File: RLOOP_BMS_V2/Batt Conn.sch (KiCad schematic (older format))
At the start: 1 part, among them J2 2-640387-0

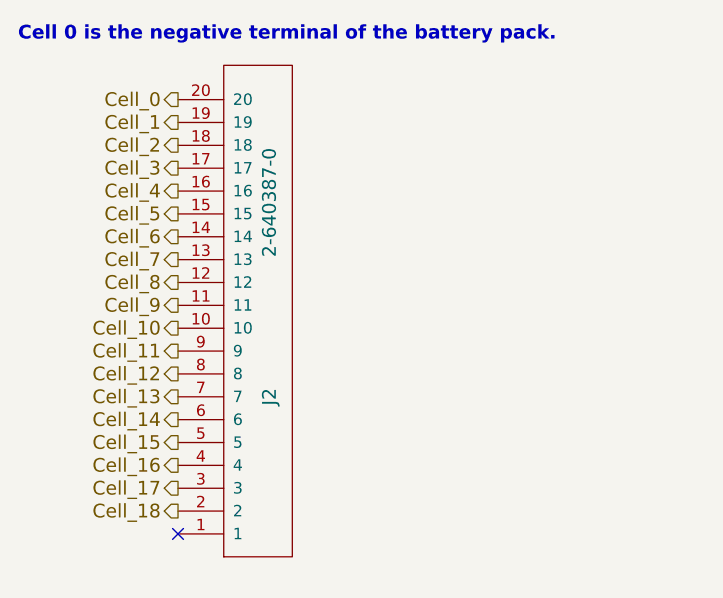
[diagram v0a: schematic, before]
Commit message: swapped a few connectors to standardize with the power node and what's readily available
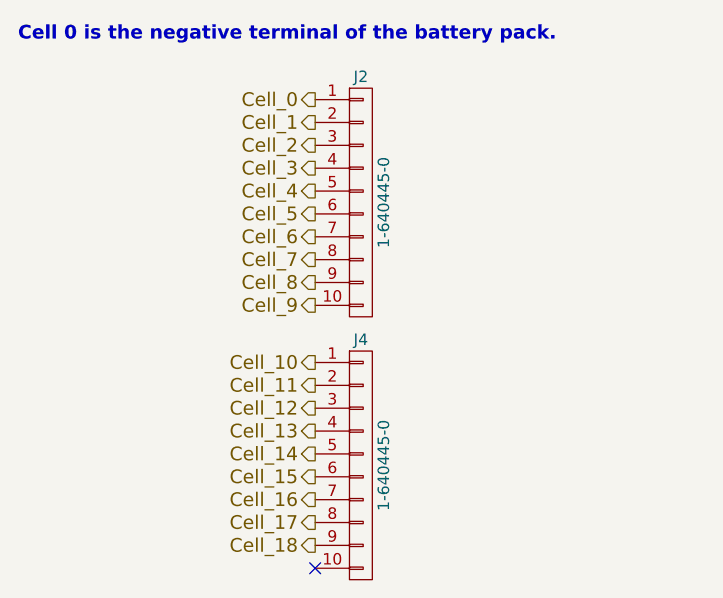
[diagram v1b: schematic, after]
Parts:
- removed J2: 2-640387-0, rLoop_Footprints:TE_2-640387-0, symbol 2-640387-0
- added J2, J4: 1-640445-0, rLoop_Footprints:1-640445-0, symbol CONN_01X10
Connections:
- net Cell_0: now also J2.1 (P1)
- net Cell_1: now also J2.2 (P2)
- net Cell_10: now also J4.1 (P1)
- net Cell_11: now also J4.2 (P2)
- net Cell_12: now also J4.3 (P3)
- net Cell_13: now also J4.4 (P4)
- net Cell_14: now also J4.5 (P5)
- net Cell_15: now also J4.6 (P6)
- net Cell_16: now also J4.7 (P7)
- net Cell_17: now also J4.8 (P8)
- net Cell_18: now also J4.9 (P9)
- net Cell_2: now also J2.3 (P3)
- net Cell_3: now also J2.4 (P4)
- net Cell_4: now also J2.5 (P5)
- net Cell_5: now also J2.6 (P6)
- net Cell_6: now also J2.7 (P7)
- net Cell_7: now also J2.8 (P8)
- net Cell_8: now also J2.9 (P9)
- net Cell_9: now also J2.10 (P10)
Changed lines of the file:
@@
 Comment4 ""
 $EndDescr
-Text HLabel 5100 2700 0    60   Output ~ 0
+Text HLabel 5700 2700 0    60   Output ~ 0
 Cell_0
-Text HLabel 5100 2800 0    60   Output ~ 0
+Text HLabel 5700 2800 0    60   Output ~ 0
 Cell_1
-Text HLabel 5100 2900 0    60   Output ~ 0
+Text HLabel 5700 2900 0    60   Output ~ 0
 Cell_2
-Text HLabel 5100 3000 0    60   Output ~ 0
+Text HLabel 5700 3000 0    60   Output ~ 0
 Cell_3
-Text HLabel 5100 3100 0    60   Output ~ 0
+Text HLabel 5700 3100 0    60   Output ~ 0
 Cell_4
-Text HLabel 5100 3200 0    60   Output ~ 0
+Text HLabel 5700 3200 0    60   Output ~ 0
 Cell_5
-Text HLabel 5100 3300 0    60   Output ~ 0
+Text HLabel 5700 3300 0    60   Output ~ 0
 Cell_6
-Text HLabel 5100 3400 0    60   Output ~ 0
+Text HLabel 5700 3400 0    60   Output ~ 0
 Cell_7
-Text HLabel 5100 3500 0    60   Output ~ 0
+Text HLabel 5700 3500 0    60   Output ~ 0
 Cell_8
-Text HLabel 5100 3600 0    60   Output ~ 0
+Text HLabel 5700 3600 0    60   Output ~ 0
 Cell_9
-Text HLabel 5100 3700 0    60   Output ~ 0
+Text HLabel 5700 3850 0    60   Output ~ 0
 Cell_10
-Text HLabel 5100 3800 0    60   Output ~ 0
+Text HLabel 5700 3950 0    60   Output ~ 0
 Cell_11
-Text HLabel 5100 3900 0    60   Output ~ 0
+Text HLabel 5700 4050 0    60   Output ~ 0
 Cell_12
-Text HLabel 5100 4000 0    60   Output ~ 0
+Text HLabel 5700 4150 0    60   Output ~ 0
 Cell_13
-Text HLabel 5100 4100 0    60   Output ~ 0
+Text HLabel 5700 4250 0    60   Output ~ 0
 Cell_14
-Text HLabel 5100 4200 0    60   Output ~ 0
+Text HLabel 5700 4350 0    60   Output ~ 0
 Cell_15
-Text HLabel 5100 4300 0    60   Output ~ 0
+Text HLabel 5700 4450 0    60   Output ~ 0
 Cell_16
-Text HLabel 5100 4400 0    60   Output ~ 0
+Text HLabel 5700 4550 0    60   Output ~ 0
 Cell_17
-Text HLabel 5100 4500 0    60   Output ~ 0
+Text HLabel 5700 4650 0    60   Output ~ 0
 Cell_18
 Text Notes 4400 2450 0    60   ~ 12
 Cell 0 is the negative terminal of the battery pack.
+NoConn ~ 5700 4750
 $Comp
-L 2-640387-0 J2
-U 1 1 5919474D
-P 5300 3650
-F 0 "J2" V 5500 4000 60  0000 C CNN
-F 1 "2-640387-0" V 5500 3150 60  0000 C CNN
-F 2 "rLoop_Footprints:TE_2-640387-0" H 5200 3150 60  0001 C CNN
-F 3 "" H 5200 3150 60  0001 C CNN
-F 4 "www.mouser.com/somethingeroher" V 5300 3650 60  0001 C CNN "Source"
-	1    5300 3650
-	1    0    0    1
+L CONN_01X10 J2
+U 1 1 595C3AE4
+P 5900 3150
+F 0 "J2" H 5900 3700 50  0000 C CNN
+F 1 "1-640445-0" V 6000 3150 50  0000 C CNN
+F 2 "rLoop_Footprints:1-640445-0" H 5900 3150 50  0001 C CNN
+F 3 "" H 5900 3150 50  0001 C CNN
+	1    5900 3150
+	1    0    0    -1
 $EndComp
-NoConn ~ 5100 4600
+$Comp
+L CONN_01X10 J4
+U 1 1 595C3B19
+P 5900 4300
+F 0 "J4" H 5900 4850 50  0000 C CNN
+F 1 "1-640445-0" V 6000 4300 50  0000 C CNN
+F 2 "rLoop_Footprints:1-640445-0" H 5900 4300 50  0001 C CNN
+F 3 "" H 5900 4300 50  0001 C CNN
+	1    5900 4300
+	1    0    0    -1
+$EndComp
 $EndSCHEMATC
